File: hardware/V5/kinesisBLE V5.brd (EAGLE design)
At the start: 122 x 86 mm, 24 parts, among them X1 JST-XH-02-PIN-ROUND-PAD, X2 JST-XH-02-PIN-ROUND-PAD

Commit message: work in progress
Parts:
- removed R4, R5: 10k, SparkFun-Resistors:AXIAL-0.3
- added JPL, JPR: (no value), pinhead:1X10
- U$4, U$5: value TOPLINKS_STAPELBERG -> MOLEX-39-53-215X-DEVMOLEX-39-53-215X-DEV; device con-molex-39-53:TOPLINKS_STAPELBERG -> nspringkeeb:MOLEX-39-53-215X-PKG
- moved R9 82.8 mm to (10.6, 63.5), turned to 90 degrees
- moved R11 79.5 mm to (8.20, 76.5), turned to 90 degrees
- moved R10 77.3 mm to (7.57, 63.5), turned to 90 degrees
- moved R12 75.5 mm to (4.86, 76.5), turned to 90 degrees
- moved C3 29.2 mm to (62.1, 49.0), turned to 270 degrees
- moved R1 21.1 mm to (82.0, 42.2)
- moved X1 16.5 mm to (11.9, 53.6), turned to 180 degrees
- moved U$1 15.7 mm to (38.8, 58.5)
- moved X2 11.3 mm to (58.1, 48.3)
- moved MCP23S17 9.20 mm to (90.8, 53.8)
- moved C1 5.24 mm to (86.1, 61.1)
- moved C2 4.89 mm to (86.3, 65.8)
- moved U$4 4.00 mm to (16.0, 31.0), flipped to the top, turned to 0 degrees
- moved U$5 4.00 mm to (106.0, 31.0)
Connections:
- net N$4 renamed ~RST
- removed net AREF: R4.P$2, R5.P$1, U$1.3
- removed net N$19: U$5.P$9
- removed net N$21: MCP23S17.8
- removed net N$24: U$5.P$4
- removed net N$44: U$4.P$5
- removed net N$50: U$4.P$11
- removed net N$54: U$6.P$13
- removed net N$55: U$6.P$11
- removed net N$56: U$6.P$12
- removed net N$57: U$6.P$10
- removed net N$58: U$6.P$9
- removed net N$60: U$6.P$7
- removed net N$61: U$6.P$6
- removed net N$67: U$7.P$1
- removed net N$68: U$7.P$2
- removed net N$75: U$7.P$9
- removed net N$76: U$7.P$10
- removed net N$77: U$7.P$11
- removed net N$78: U$7.P$12
- removed net N$79: U$7.P$13
- net 3V@1: now also U$1.3
- net COL-B: now also U$5.P$7@2
- net COL-C: now also JPL.2
- net COL-D: now also JPL.8
- net COL-E: now also JPL.1, U$5.P$11@2
- net COL-F: now also JPL.3
- net COL-G: now also JPR.3, U$4.P$1@2
- net COL-H: now also JPR.4, U$4.P$3@2
- net COL-I: now also JPR.5
- net COL-J: now also JPR.6
- net COL-K: now also U$4.P$13@2
- net GND: no longer R5.P$2
- net N$5: no longer R4.P$1
- net ROW-1: now also U$5.P$13@2
- net ROW-2: now also U$4.P$9@2, U$5.P$5@2
- net ROW-3: now also U$5.P$3@2
- net ROW-4: now also U$4.P$7@2
- net ROW-5: now also U$5.P$1@2
- net ROW-6: now also JPL.5, JPR.8
- net ROW-7: now also JPL.4, JPR.7
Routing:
- net KEY: track 271.4 -> 33.3 mm
- net SCR: track 258.0 -> 31.0 mm
- net GND: track 299.3 -> 80.4 mm
- net NUM: track 250.5 -> 66.4 mm
- net CAPS: track 239.8 -> 65.6 mm
- net N$11: track 11.5 -> 123.3 mm
- net N$10: track 11.2 -> 118.4 mm
- net N$1: track 11.2 -> 118.3 mm
- net N$12: track 11.2 -> 108.4 mm
- net COL-J: track 190.0 -> 102.3 mm
- net ROW-5: track 197.9 -> 131.4 mm
- net ROW-1: track 166.0 -> 107.3 mm, vias 0 -> 1
- net ROW-3: track 169.6 -> 112.1 mm, vias 0 -> 1
- net ROW-2: track 166.8 -> 113.1 mm, vias 0 -> 1
- net COL-I: track 158.0 -> 104.5 mm
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
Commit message: first cut routing
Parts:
- moved R12 66.3 mm to (22.8, 12.7), turned to 180 degrees
- moved R11 63.2 mm to (22.8, 15.1), turned to 180 degrees
- moved JPR 4.50 mm to (21.1, 3.30)
- moved JPL 0.51 mm to (102.4, 3.30)
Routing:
- net COL-G: track 62.5 -> 166.6 mm
- net N$11: track 123.3 -> 33.6 mm
- net ROW-3: track 112.1 -> 201.4 mm, vias 1 -> 2
- net N$12: track 108.4 -> 22.4 mm
- net ROW-2: track 113.1 -> 196.6 mm, vias 1 -> 2
- net KEY: track 33.3 -> 113.0 mm
- net SCR: track 31.0 -> 108.4 mm
- net ROW-1: track 107.3 -> 182.3 mm
- net COL-E: track 26.1 -> 76.7 mm
- net COL-C: track 11.3 -> 55.5 mm
- net COL-I: track 104.5 -> 146.7 mm
- net COL-B: track 0.00 -> 29.3 mm
- net COL-A: track 0.00 -> 26.5 mm
- net ROW-5: track 131.4 -> 156.1 mm, vias 1 -> 2
- net COL-J: track 102.3 -> 125.6 mm
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
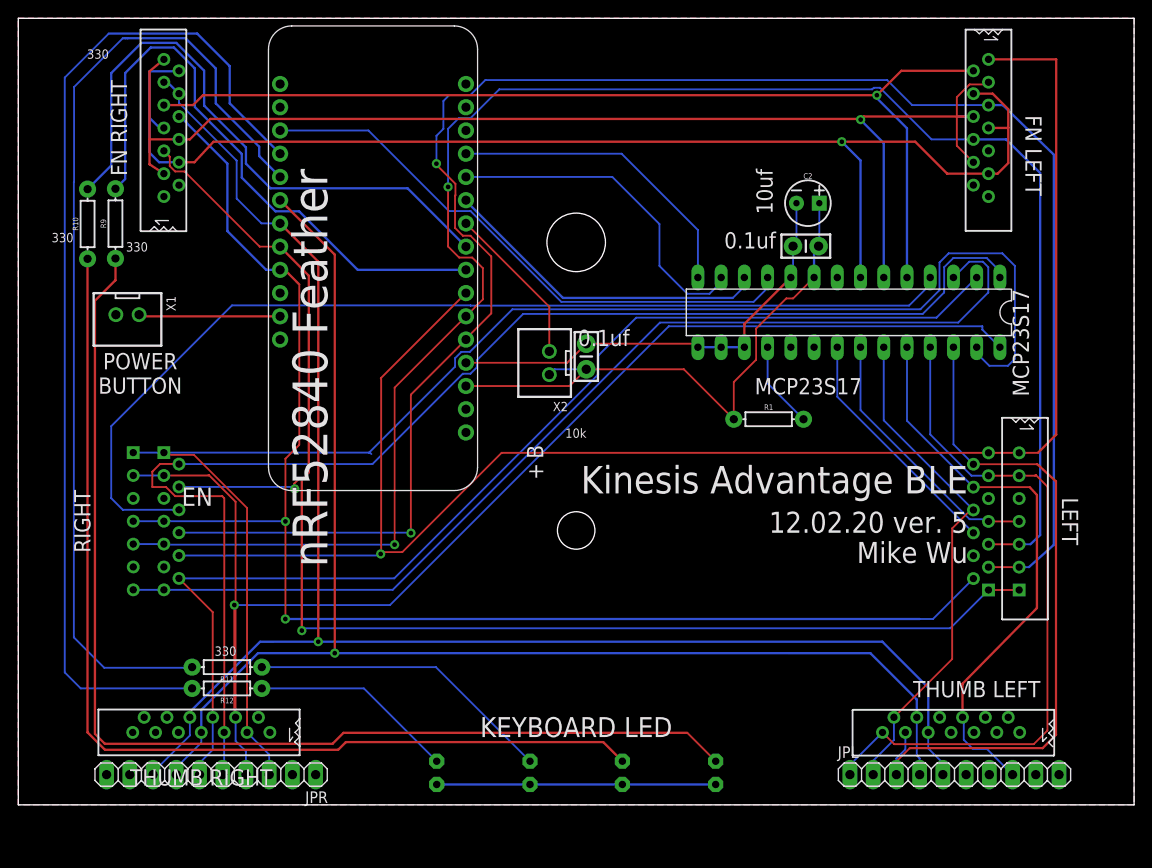
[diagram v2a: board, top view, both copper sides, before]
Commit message: minor reroute, ERC fixes
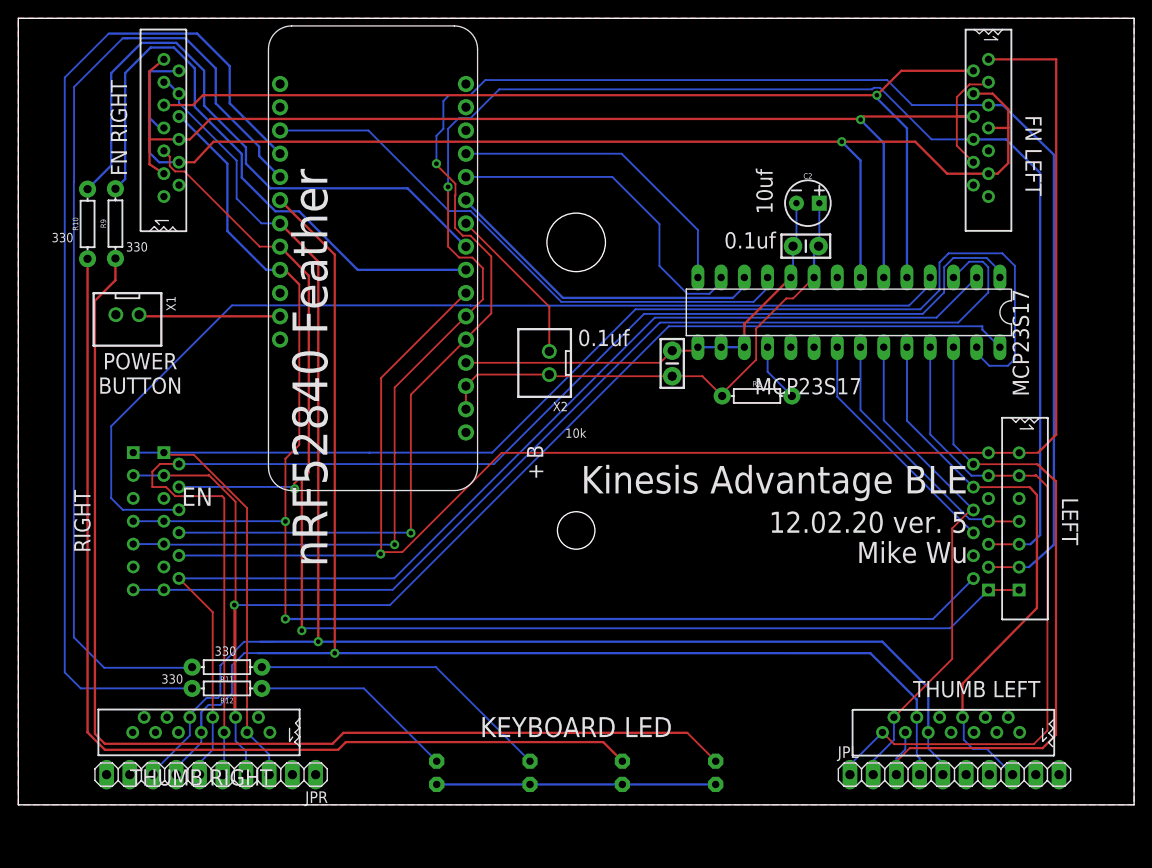
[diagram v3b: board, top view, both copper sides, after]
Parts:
- JPL, JPR: value (none) -> 10
- moved C3 9.43 mm to (71.5, 48.3)
- moved R1 2.84 mm to (80.8, 44.7)
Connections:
- removed net N$5: U$1.26
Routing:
- net 3V@1: track 64.7 -> 58.1 mm
- net ~RST: track 9.50 -> 6.43 mm
- net ROW-6: track 174.3 -> 176.6 mm
- net ROW-7: track 151.5 -> 153.1 mm
- net COL-J: track 125.6 -> 124.4 mm
- net COL-G: track 166.6 -> 165.8 mm

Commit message: updates to power trace width, spacing
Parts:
- moved R9 11.0 mm to (14.2, 53.1), turned to 0 degrees
- moved X1 10.8 mm to (20.8, 47.5), turned to 270 degrees
- moved R10 10.1 mm to (14.2, 55.9), turned to 0 degrees
- moved X2 3.30 mm to (54.8, 48.3)
- moved C3 1.30 mm to (71.2, 47.0)
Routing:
- net GND: track 80.1 -> 207.8 mm
- net CAPS: track 65.6 -> 38.1 mm
- net ROW-3: track 201.4 -> 173.9 mm
- net NUM: track 66.4 -> 39.5 mm
- net ROW-2: track 196.6 -> 179.2 mm
- net COL-H: track 152.6 -> 139.1 mm
- net N$1: track 123.0 -> 115.4 mm
- net EN: track 15.9 -> 10.1 mm
- net KEY: track 113.0 -> 108.7 mm
- net SS: track 62.8 -> 66.4 mm
- net SCR: track 108.4 -> 105.4 mm
- net SCK: track 36.4 -> 39.1 mm
- net N$10: track 112.3 -> 109.7 mm
- net COL-N: track 137.4 -> 139.5 mm
- net COL-L: track 112.6 -> 110.7 mm
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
